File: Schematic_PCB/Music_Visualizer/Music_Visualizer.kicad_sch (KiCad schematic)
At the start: 149 parts, among them J1 AudioJack3, J3 Screw_Terminal_01x02, SW1 SW_SPDT, U1 LM324, U2 LM324, U3 LM324, U4 LM324, U5 LM324, U6 LM324, U7 LM324

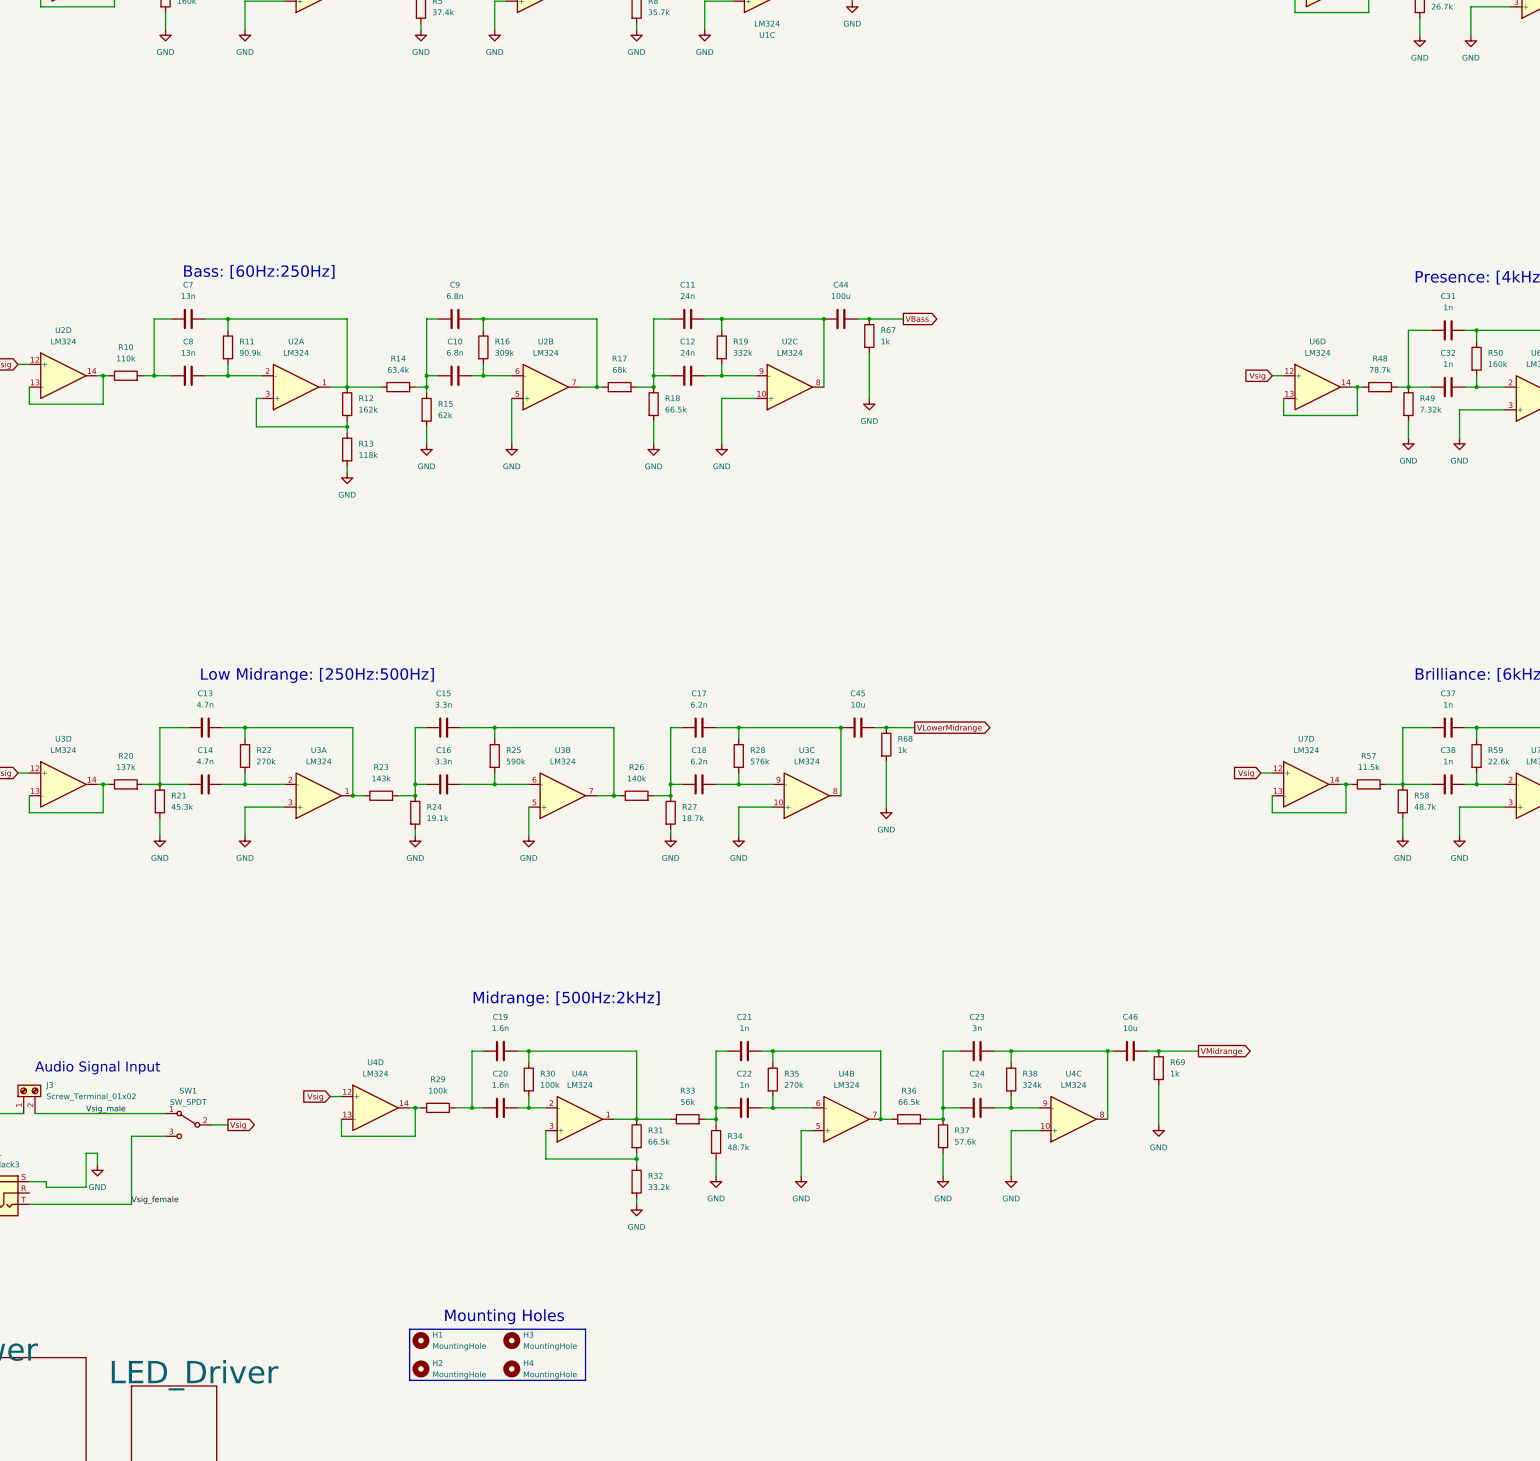
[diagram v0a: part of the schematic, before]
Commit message: RHi- Value controll replaced
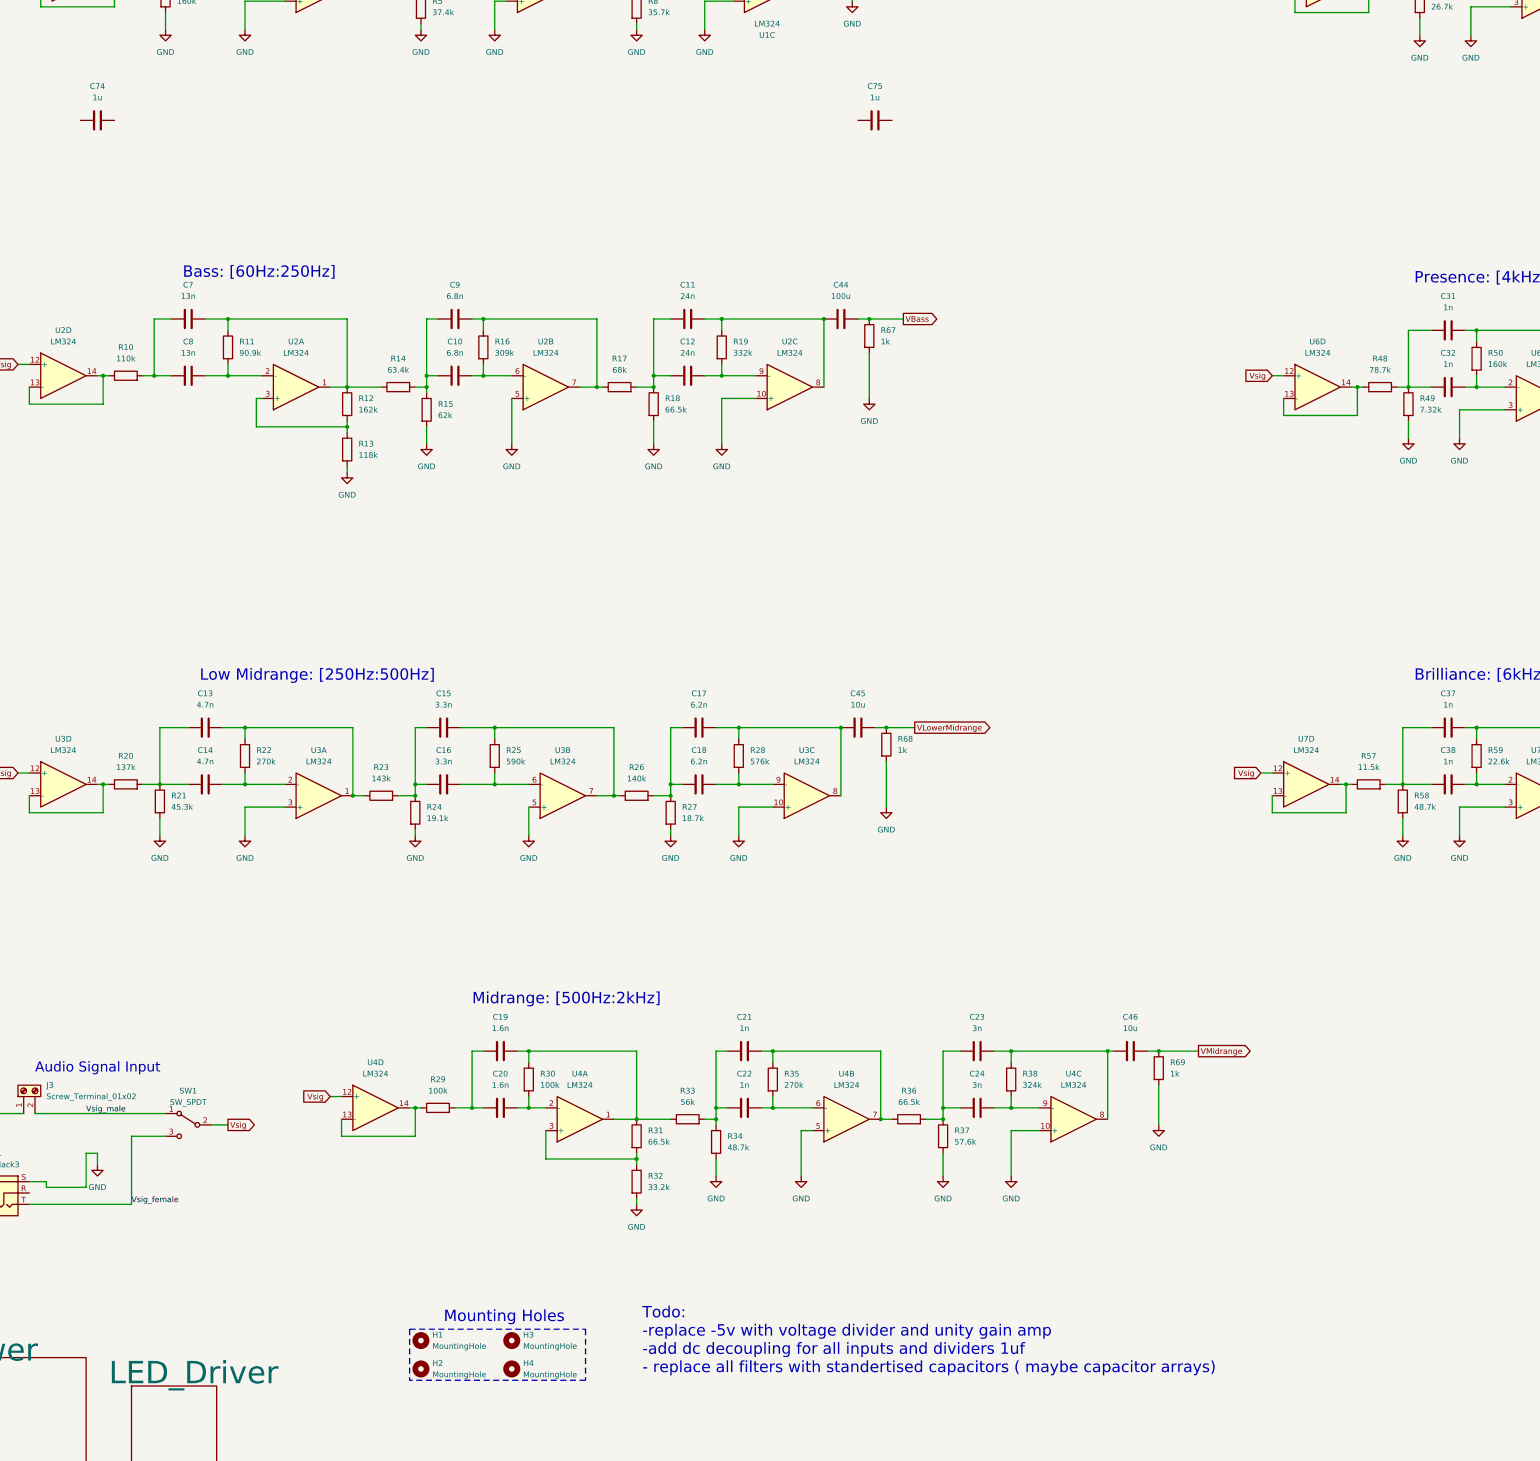
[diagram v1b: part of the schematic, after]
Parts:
- added C74, C75: 1u, Capacitor_SMD:C_0603_1608Metric_Pad1.08x0.95mm_HandSolder, symbol Device:C
- U1, U2, U3, U4, U5, U6, U7: Spice_Lib_File lmx24_lm2902-quad.lib -> (none); Spice_Model LMX24_LM2902a -> (none); Spice_Netlist_Enabled Y -> (none); Spice_Primitive X -> (none)
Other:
- note added: "Todo: -replace -5v with voltage divider and unity gain amp -add dc decoupling for all inputs and dividers 1uf - replace all filters with standertised capacitors ( maybe capacitor arrays)"

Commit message: Replace +-5v with 9v
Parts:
- removed C10, C9: 6.8n, Capacitor_SMD:C_0805_2012Metric, symbol Device:C
- removed C11, C12: 24n, Capacitor_SMD:C_0805_2012Metric, symbol Device:C
- removed C13, C14: 4.7n, Capacitor_SMD:C_0603_1608Metric_Pad1.08x0.95mm_HandSolder, symbol Device:C
- removed C15, C16: 3.3n, Capacitor_SMD:C_0603_1608Metric_Pad1.08x0.95mm_HandSolder, symbol Device:C
- removed C17, C18: 6.2n, Capacitor_SMD:C_0805_2012Metric, symbol Device:C
- removed C19, C20: 1.6n, Capacitor_SMD:C_0603_1608Metric_Pad1.08x0.95mm_HandSolder, symbol Device:C
- removed C21, C22, C25, C26, C27, C28, C29, C30, C31, C32, C33, C34, C35, C36, C37, C38, C41, C42: 1n, Capacitor_SMD:C_0603_1608Metric_Pad1.08x0.95mm_HandSolder, symbol Device:C
- removed C23, C24: 3n, Capacitor_SMD:C_0603_1608Metric_Pad1.08x0.95mm_HandSolder, symbol Device:C
- removed C39, C40: 820p, Capacitor_SMD:C_0603_1608Metric_Pad1.08x0.95mm_HandSolder, symbol Device:C
- removed C44: 100u, Capacitor_SMD:C_1206_3216Metric, symbol Device:C
- removed C45, C46: 10u, Capacitor_SMD:C_0805_2012Metric, symbol Device:C
- removed C47, C48, C49, C74, C75: 1u, Capacitor_SMD:C_0603_1608Metric_Pad1.08x0.95mm_HandSolder, symbol Device:C
- removed C7, C8: 13n, Capacitor_SMD:C_0805_2012Metric, symbol Device:C
- removed R10: 110k, Resistor_SMD:R_0603_1608Metric_Pad0.98x0.95mm_HandSolder, symbol Device:R
- removed R11, R65: 90.9k, Resistor_SMD:R_0603_1608Metric_Pad0.98x0.95mm_HandSolder, symbol Device:R
- removed R12: 162k, Resistor_SMD:R_0603_1608Metric_Pad0.98x0.95mm_HandSolder, symbol Device:R
- removed R13: 118k, Resistor_SMD:R_0603_1608Metric_Pad0.98x0.95mm_HandSolder, symbol Device:R
- removed R14: 63.4k, Resistor_SMD:R_0603_1608Metric_Pad0.98x0.95mm_HandSolder, symbol Device:R
- removed R15: 62k, Resistor_SMD:R_0603_1608Metric_Pad0.98x0.95mm_HandSolder, symbol Device:R
- removed R16: 309k, Resistor_SMD:R_0603_1608Metric_Pad0.98x0.95mm_HandSolder, symbol Device:R
- removed R17: 68k, Resistor_SMD:R_0603_1608Metric_Pad0.98x0.95mm_HandSolder, symbol Device:R
- removed R18, R31, R36, R51: 66.5k, Resistor_SMD:R_0603_1608Metric_Pad0.98x0.95mm_HandSolder, symbol Device:R
- removed R19: 332k, Resistor_SMD:R_0603_1608Metric_Pad0.98x0.95mm_HandSolder, symbol Device:R
- removed R20: 137k, Resistor_SMD:R_0603_1608Metric_Pad0.98x0.95mm_HandSolder, symbol Device:R
- removed R21: 45.3k, Resistor_SMD:R_0603_1608Metric_Pad0.98x0.95mm_HandSolder, symbol Device:R
- removed R22, R35, R53: 270k, Resistor_SMD:R_0603_1608Metric_Pad0.98x0.95mm_HandSolder, symbol Device:R
- removed R23: 143k, Resistor_SMD:R_0603_1608Metric_Pad0.98x0.95mm_HandSolder, symbol Device:R
- removed R24: 19.1k, Resistor_SMD:R_0603_1608Metric_Pad0.98x0.95mm_HandSolder, symbol Device:R
- removed R25: 590k, Resistor_SMD:R_0603_1608Metric_Pad0.98x0.95mm_HandSolder, symbol Device:R
- removed R26: 140k, Resistor_SMD:R_0603_1608Metric_Pad0.98x0.95mm_HandSolder, symbol Device:R
- removed R27: 18.7k, Resistor_SMD:R_0603_1608Metric_Pad0.98x0.95mm_HandSolder, symbol Device:R
- removed R28: 576k, Resistor_SMD:R_0603_1608Metric_Pad0.98x0.95mm_HandSolder, symbol Device:R
- removed R29, R30: 100k, Resistor_SMD:R_0603_1608Metric_Pad0.98x0.95mm_HandSolder, symbol Device:R
- removed R32: 33.2k, Resistor_SMD:R_0603_1608Metric_Pad0.98x0.95mm_HandSolder, symbol Device:R
- removed R33: 56k, Resistor_SMD:R_0603_1608Metric_Pad0.98x0.95mm_HandSolder, symbol Device:R
- removed R34, R58: 48.7k, Resistor_SMD:R_0603_1608Metric_Pad0.98x0.95mm_HandSolder, symbol Device:R
- removed R37: 57.6k, Resistor_SMD:R_0603_1608Metric_Pad0.98x0.95mm_HandSolder, symbol Device:R
- removed R38: 324k, Resistor_SMD:R_0603_1608Metric_Pad0.98x0.95mm_HandSolder, symbol Device:R
- removed R39, R48: 78.7k, Resistor_SMD:R_0603_1608Metric_Pad0.98x0.95mm_HandSolder, symbol Device:R
- removed R40: 26.7k, Resistor_SMD:R_0603_1608Metric_Pad0.98x0.95mm_HandSolder, symbol Device:R
- removed R41, R50: 160k, Resistor_SMD:R_0603_1608Metric_Pad0.98x0.95mm_HandSolder, symbol Device:R
- removed R42: 59k, Resistor_SMD:R_0603_1608Metric_Pad0.98x0.95mm_HandSolder, symbol Device:R
- removed R43: 7.87k, Resistor_SMD:R_0603_1608Metric_Pad0.98x0.95mm_HandSolder, symbol Device:R
- removed R44: 243k, Resistor_SMD:R_0603_1608Metric_Pad0.98x0.95mm_HandSolder, symbol Device:R
- removed R45: 107k, Resistor_SMD:R_0603_1608Metric_Pad0.98x0.95mm_HandSolder, symbol Device:R
- removed R46: 14.7k, Resistor_SMD:R_0603_1608Metric_Pad0.98x0.95mm_HandSolder, symbol Device:R
- removed R47: 453k, Resistor_SMD:R_0603_1608Metric_Pad0.98x0.95mm_HandSolder, symbol Device:R
- removed R49: 7.32k, Resistor_SMD:R_0603_1608Metric_Pad0.98x0.95mm_HandSolder, symbol Device:R
- removed R52: 2.87k, Resistor_SMD:R_0603_1608Metric_Pad0.98x0.95mm_HandSolder, symbol Device:R
- removed R54: 95.3k, Resistor_SMD:R_0603_1608Metric_Pad0.98x0.95mm_HandSolder, symbol Device:R
- removed R55: 4.02k, Resistor_SMD:R_0603_1608Metric_Pad0.98x0.95mm_HandSolder, symbol Device:R
- removed R56: 383k, Resistor_SMD:R_0603_1608Metric_Pad0.98x0.95mm_HandSolder, symbol Device:R
- removed R57: 11.5k, Resistor_SMD:R_0805_2012Metric, symbol Device:R
- removed R59: 22.6k, Resistor_SMD:R_0603_1608Metric_Pad0.98x0.95mm_HandSolder, symbol Device:R
- removed R60: 8.06k, Resistor_SMD:R_0603_1608Metric_Pad0.98x0.95mm_HandSolder, symbol Device:R
- removed R61: 4.32k, Resistor_SMD:R_0603_1608Metric_Pad0.98x0.95mm_HandSolder, symbol Device:R
- removed R62: 37.4k, Resistor_SMD:R_0603_1608Metric_Pad0.98x0.95mm_HandSolder, symbol Device:R
- removed R63: 19.6k, Resistor_SMD:R_0603_1608Metric_Pad0.98x0.95mm_HandSolder, symbol Device:R
- removed R64: 10.7k, Resistor_SMD:R_0603_1608Metric_Pad0.98x0.95mm_HandSolder, symbol Device:R
- removed R67, R68, R69, R70, R71, R72: 1k, Resistor_SMD:R_0603_1608Metric_Pad0.98x0.95mm_HandSolder, symbol Device:R
- removed unit 1 of U2
- removed unit 3 of U2
- removed unit 2 of U2
- removed unit 4 of U2
- removed unit 2 of U3
- removed unit 1 of U3
- removed unit 3 of U3
- removed unit 4 of U3
- removed unit 1 of U4
- removed unit 2 of U4
- removed unit 4 of U4
- removed unit 3 of U4
- removed unit 3 of U5
- removed unit 1 of U5
- removed unit 4 of U5
- removed unit 2 of U5
- removed unit 1 of U6
- removed unit 4 of U6
- removed unit 2 of U6
- removed unit 3 of U6
- removed unit 3 of U7
- removed unit 2 of U7
- removed unit 4 of U7
- removed unit 1 of U7
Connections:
- net -5V: no longer C61.1, C63.1, C65.1, C67.1, C69.1, C71.1, U1.11 (V-), U2.11 (V-), U3.11 (V-), U4.11 (V-), U5.11 (V-), U6.11 (V-)
- net GND: now also C61.1, C63.1, C65.1, C67.1, C69.1, C71.1, U1.11 (V-), U2.11 (V-), U3.11 (V-), U4.11 (V-), U5.11 (V-), U6.11 (V-); no longer R2.2, R5.2, R8.2, U1.10 (+), U1.3 (+), U1.5 (+)
- net +5V renamed +9V
- new net VCC4_5: R2.2, R5.2, R8.2, U1.10 (+), U1.3 (+), U1.5 (+)
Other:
- note added: "Jamaina"
- note added: "Op-Amp Power"
- note added: "Todo: -add dc decoupling for all inputs and dividers 1uf - replace all filters with standertised capacitors ( maybe capacitor arrays) Done --replace -5v with voltage divider and unity gain amp-"
- note removed: "Op-Amp Power (+/-5V)"
- note removed: "Todo: -replace -5v with voltage divider and unity gain amp -add dc decoupling for all inputs and dividers 1uf - replace all filters with standertised capacitors ( maybe capacitor arrays)"

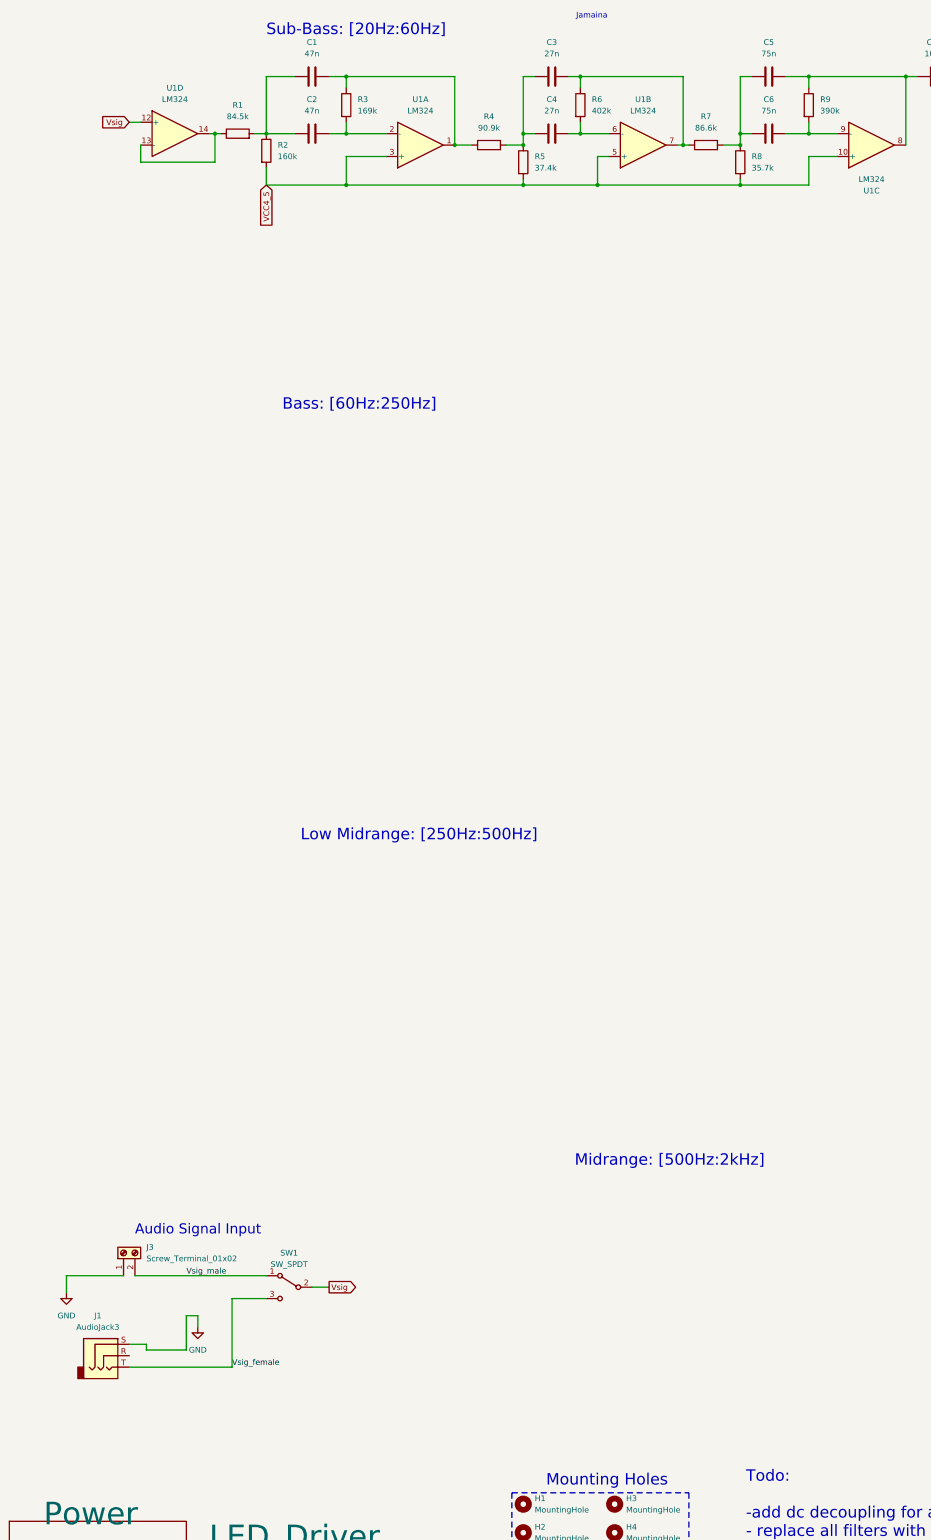
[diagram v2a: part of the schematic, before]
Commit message: Input buffer 20-60hz filter changed
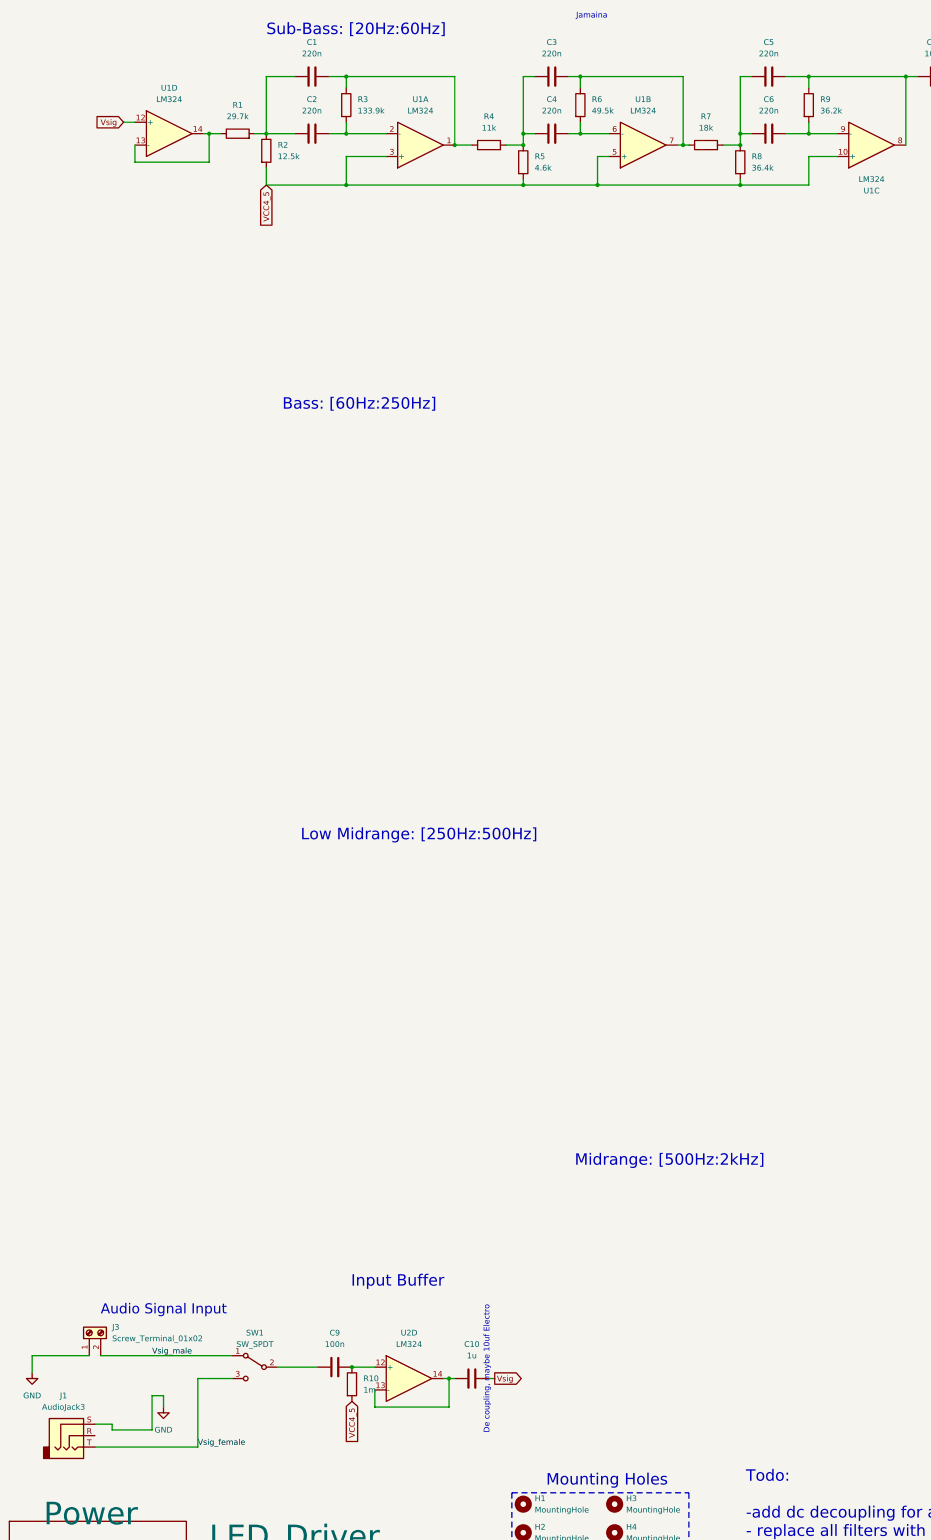
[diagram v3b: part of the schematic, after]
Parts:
- added C10: 1u, Capacitor_SMD:C_0603_1608Metric_Pad1.08x0.95mm_HandSolder, symbol Device:C
- added C9: 100n, Capacitor_SMD:C_0603_1608Metric_Pad1.08x0.95mm_HandSolder, symbol Device:C
- added R10: 1m, Resistor_SMD:R_0603_1608Metric_Pad0.98x0.95mm_HandSolder, symbol Device:R
- added unit 4 of U2
- C1, C2: value 47n -> 220n
- C3, C4: value 27n -> 220n
- C5, C6: value 75n -> 220n
- R1: value 84.5k -> 29.7k
- R2: value 160k -> 12.5k
- R3: value 169k -> 133.9k
- R4: value 90.9k -> 11k
- R5: value 37.4k -> 4.6k
- R6: value 402k -> 49.5k
- R7: value 86.6k -> 18k
- R8: value 35.7k -> 36.4k
- R9: value 390k -> 36.2k
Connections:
- net VCC4_5: now also R10.2
- net Vsig: now also C10.2; no longer SW1.2 (B)
- new net: C9.2, R10.1, U2.12 (+)
- new net: C10.1, U2.13 (-), U2.14
- new net: C9.1, SW1.2 (B)
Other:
- note added: "De coupling, maybe 10uf Electro"
- note added: "Input Buffer"
- moved on the sheet: J1, J3, SW1, U1D
